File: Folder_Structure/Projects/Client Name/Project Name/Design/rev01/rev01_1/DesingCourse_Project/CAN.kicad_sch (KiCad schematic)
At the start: 11 parts, among them J10 874380443, U5 SN65HVD230D

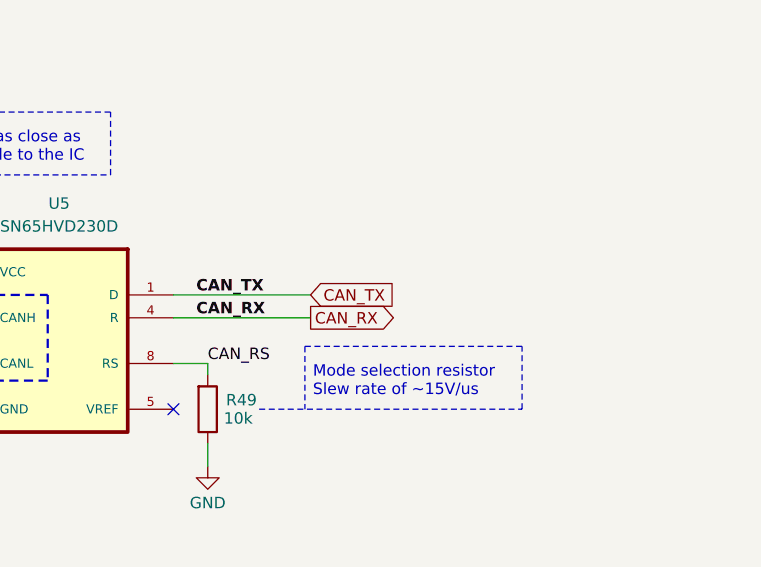
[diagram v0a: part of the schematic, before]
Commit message: Update19
PCB finished before applying curved traces
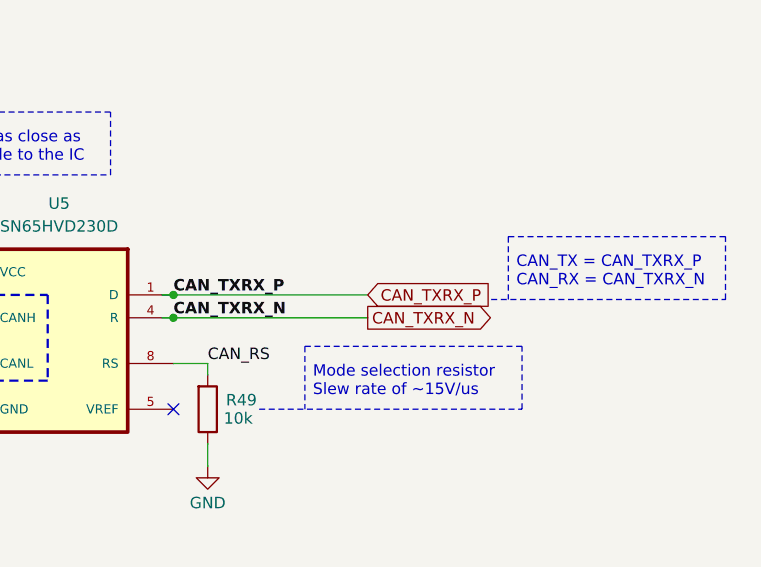
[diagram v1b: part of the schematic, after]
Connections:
- net CAN_RX renamed CAN_TXRX_N
- net CAN_TX renamed CAN_TXRX_P
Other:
- note added: "CAN_TX = CAN_TXRX_P CAN_RX = CAN_TXRX_N"
